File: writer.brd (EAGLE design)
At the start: 59.7 x 36.8 mm, 12 parts, among them T1 2SC1815, T2 2SC1815

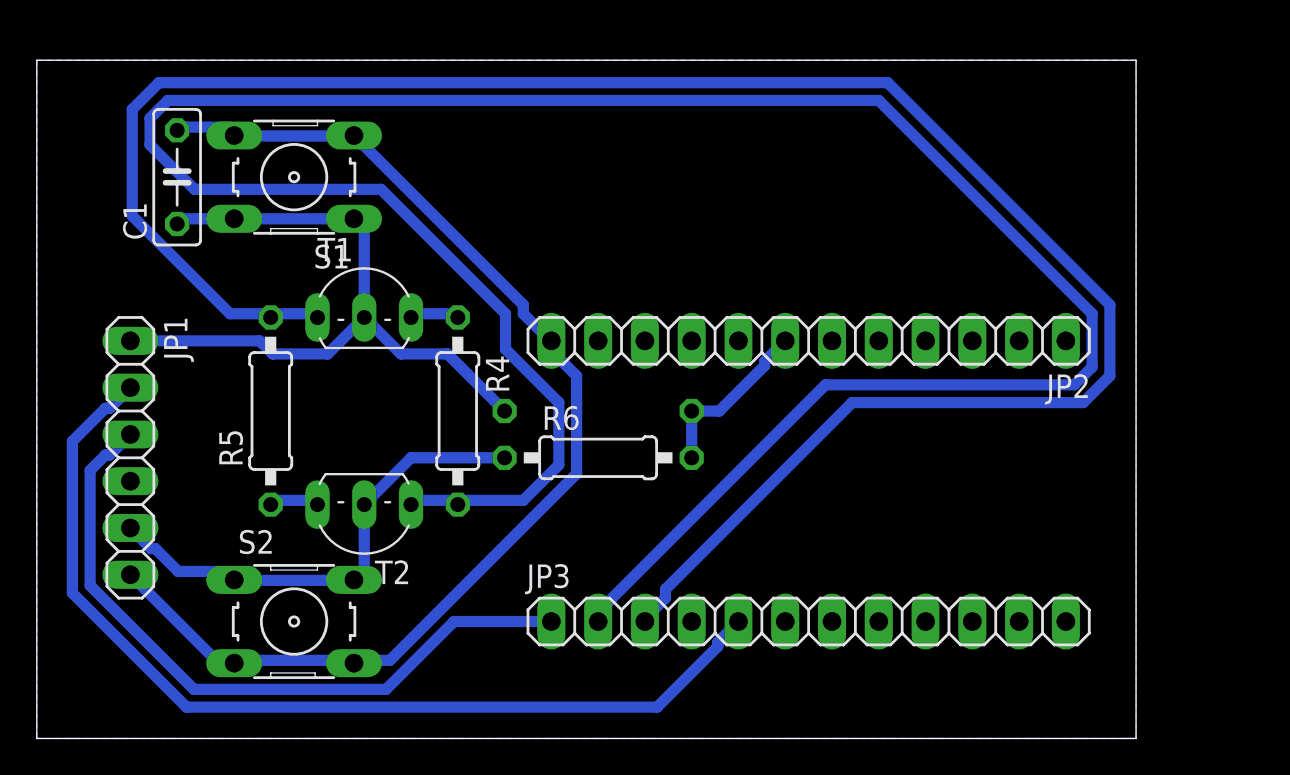
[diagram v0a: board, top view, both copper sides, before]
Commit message: feat: remove unnecessary resister & adjust layout
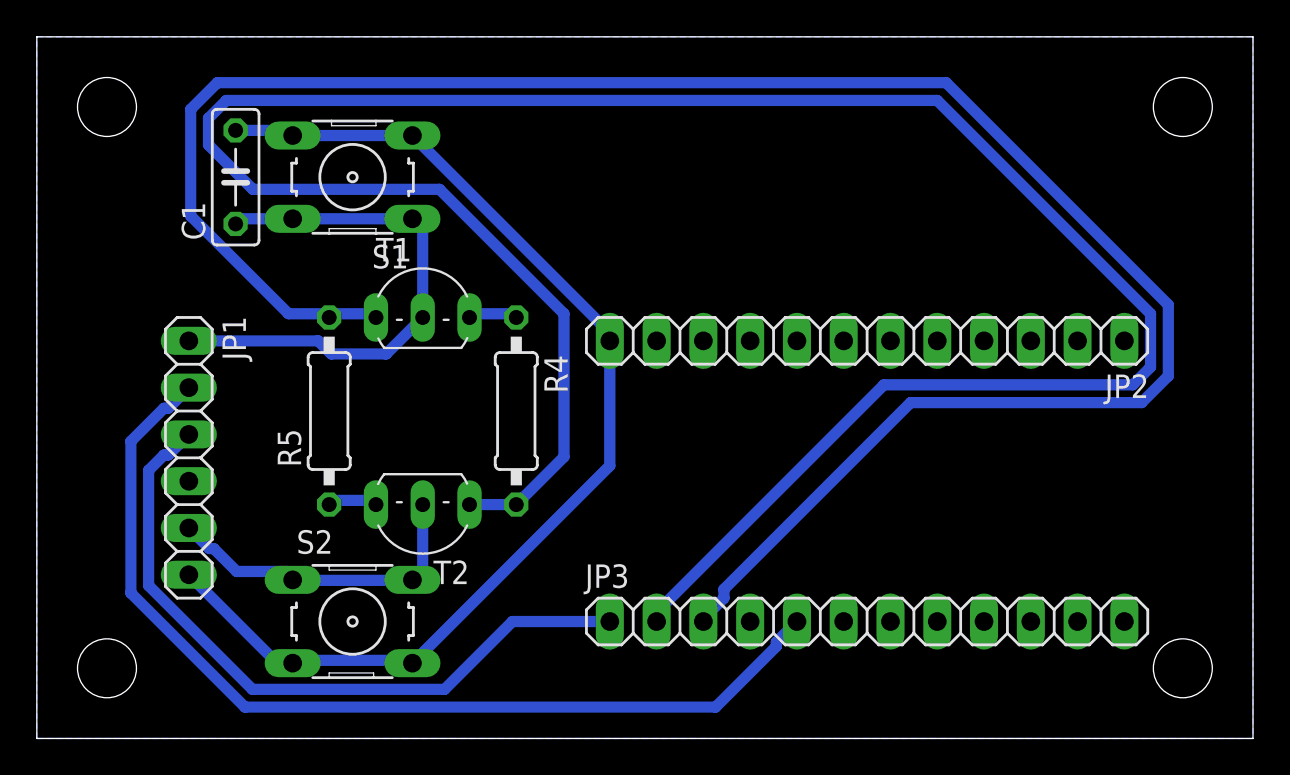
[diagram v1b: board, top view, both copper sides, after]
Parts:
- removed R1, R6: 10k, rcl:0207/10
- moved JP2 3.18 mm to (45.1, 21.6)
- moved JP3 3.18 mm to (45.1, 6.35)
- moved JP1 3.18 mm to (8.26, 15.2)
- moved R4 3.18 mm to (26.0, 17.8)
- moved R5 3.18 mm to (15.9, 17.8)
- moved C1 3.17 mm to (10.8, 30.5)
- moved S1 3.17 mm to (17.1, 30.5)
- moved S2 3.17 mm to (17.1, 6.35)
- moved T1 3.17 mm to (21.0, 22.9)
- moved T2 3.17 mm to (21.0, 12.7)
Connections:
- net +3V3: no longer R1.2, R6.2
- net BOOT: no longer R6.1
- net EN: no longer R1.1
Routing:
- net EN: track 38.8 -> 29.1 mm
- net +3V3: track 9.33 -> 0.00 mm
- net BOOT: track 26.4 -> 17.7 mm
- net DTR: track 135.1 -> 130.6 mm
- net GND: track 64.0 -> 61.6 mm
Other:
- board size 59.7 x 36.8 mm -> 66 x 38.1 mm
